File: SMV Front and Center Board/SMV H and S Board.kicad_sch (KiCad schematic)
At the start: 55 parts, among them J1 430450200, J10 Molex Micro-Fit 4 Pin, J2 430450200, J3 XT60-M, J4 22035035, J7 22035035, J8 22035035, J9 22035035, Q1 PSMN1R8-40YLC_115 - MOSFET, Q3 PSMN1R8-40YLC_115 - MOSFET, U1 UA78M05QDCYRG4Q1, U3 PADS131M04QPWRQ1

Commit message: PCB First Layout
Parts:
- removed C3: 220 nF, symbol Device:C
- removed J8, J9: 22035035, CON_22035035_MOL, symbol SMV_Custom:3-pin Mini Molex Spox
- removed Q3: PSMN1R8-40YLC_115 - MOSFET, LFPAK56_SOT669_NEX, symbol PSMN1R8-40YLC,115:PSMN1R8-40YLC_115
- added C1: C0805C224K3RACTU, SMV_Passives:Cap0805, symbol SMV_Custom:C0805C224K3RACTU
- added J5, J6: 22035035, SMV_Connectors:3pin_CON_22035035_MOL, symbol SMV_Custom:3-pin Mini Molex Spox
- added Q2: PSMN1R8-40YLC_115, LFPAK56_SOT669_NEX, symbol PSMN1R8-40YLC,115:PSMN1R8-40YLC_115
- added TP17, TP18: 3V3A, TestPoint:TestPoint_Pad_D3.0mm, symbol Connector:TestPoint
- J4, J7: footprint CON_22035035_MOL -> SMV_Connectors:3pin_CON_22035035_MOL
- Q1: value PSMN1R8-40YLC_115 - MOSFET -> PSMN1R8-40YLC_115
- TP11, TP16: value TestPoint -> 3V3A; footprint (none) -> TestPoint:TestPoint_Pad_D3.0mm
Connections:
- net +3.3V: now also J7.1
- net +3V3: now also RP2040.26 (3.3V), RP2040.27 (3.3V); no longer RP2040.14, RP2040.15
- net CAN_H: now also RP2040.31 (CAN_H), J5.1, J6.1, TP18.1; no longer J7.1, RP2040.1
- net CAN_L: now also RP2040.29 (CAN_L), TP16.1, J5.3, J6.3; no longer J7.3, RP2040.3
- net D1: now also Q2.5; no longer Q1.5
- net D2: now also Q1.5
- net D25: now also RP2040.19 (D25); no longer RP2040.7
- net D4: now also RP2040.13 (D4); no longer RP2040.1
- net GND: now also Q1.1, Q1.2, Q1.3, RP2040.25 (GND), RP2040.30 (GND), C1.2, J5.2, J6.2; no longer RP2040.13, RP2040.2
- net GND - S: now also Q2.1, Q2.2, Q2.3; no longer Q1.1, Q1.2, Q1.3
- net MISO: now also RP2040.16 (MISO), TP17.1; no longer RP2040.4, TP16.1
- net MOSI: now also RP2040.17 (MOSI); no longer RP2040.5
- net SCLK: now also RP2040.18 (SCK); no longer RP2040.6
- net at R2.2, R7.2: now also Q1.4
- net at U3.18 (CAP): now also C1.1
- net at R13.1, TP13.1: now also J4.3
- net at R15.2, TP14.1: now also J7.3; no longer J4.3
- net at R12.2: now also RP2040.23 (A1); no longer RP2040.11
- net at R11.2: now also RP2040.24 (A0); no longer RP2040.12
- net at R3.1, R8.2: now also Q2.4; no longer Q1.4
- no-connect marks 16 -> 15

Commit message: PCB Layout Draft and Small Schematic Changes
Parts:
- added TP19, TP20, TP21: 3V3A, TestPoint:TestPoint_Pad_D3.0mm, symbol Connector:TestPoint
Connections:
- net CS: now also RP2040.21 (A3), TP19.1; no longer RP2040.4 (D13)
- net GND: now also D2.1
- net MISO: now also RP2040.22 (A2); no longer RP2040.16 (MISO)
- net MOSI: now also RP2040.23 (A1); no longer RP2040.17 (MOSI)
- net SCLK: now also TP21.1
- net GPIO_RESET: now reaches RP2040.20 (D24)
- net GPIO_RESET: now also U3.11 (SYNC/RESET), TP20.1
- net at R12.2: now also RP2040.9 (D6); no longer RP2040.23 (A1)
- net at R11.2: now also RP2040.7 (D10); no longer RP2040.24 (A0)
- net D12: now reaches RP2040.5 (D12)
- net D12: now also R8.1
- net D25: no longer names the net of RP2040.19 (D25)
- net D25: no longer R7.1
- net D4: no longer names the net of RP2040.13 (D4)
- net D4: no longer R8.1
- net PWM_OUT: no longer names the net of RP2040.12 (SDA)
- net PWM_OUT: no longer U3.17 (CLKIN)
- net TX1 renamed D11
- net D11: now also R7.1; no longer U3.11 (SYNC/RESET)
- new net GPIO_CLKIN: RP2040.24 (A0), U3.17 (CLKIN)
- no-connect marks 15 -> 9
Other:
- moved on the sheet: D1, D2, R11, R12

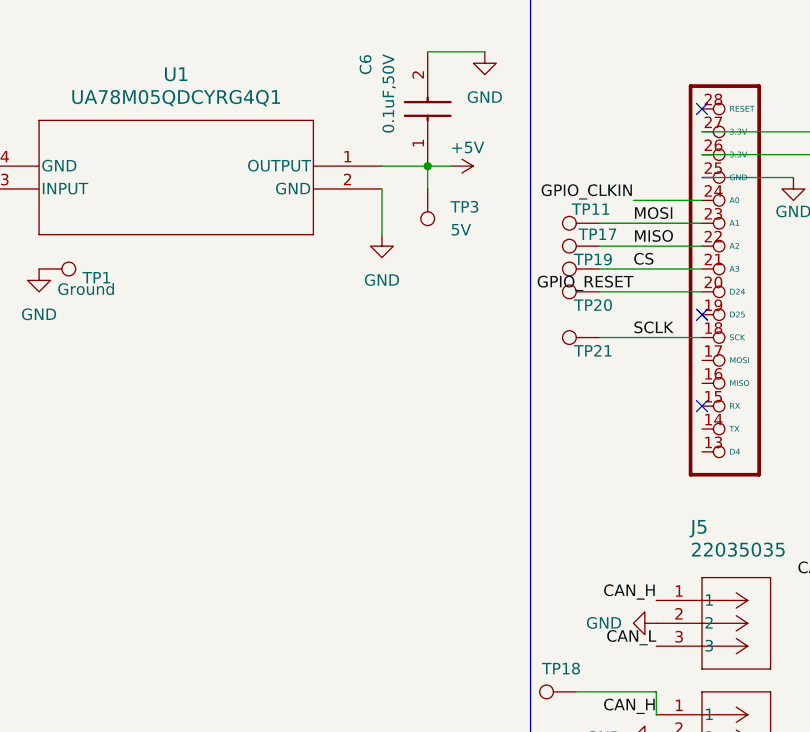
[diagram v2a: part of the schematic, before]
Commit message: Formed compact subsystems
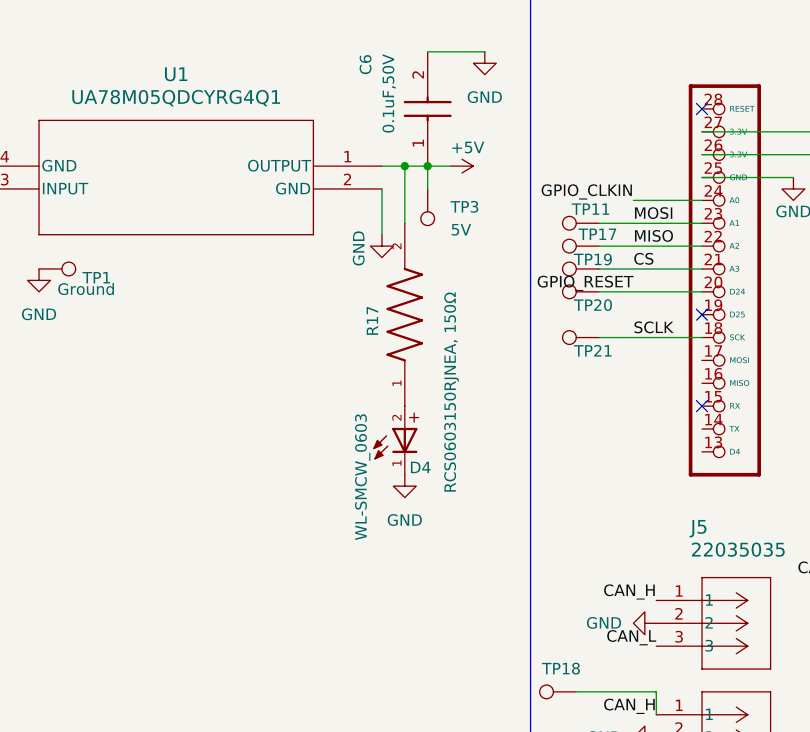
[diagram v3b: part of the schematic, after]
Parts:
- added D4: WL-SMCW_0603, SMV_Passives:WL-SMCW_0603(diode), symbol SMV_Custom:WL-SMCW_0603
- added R17: RCS0603150RJNEA, 150Ω, SMV_Passives:0805RESC2012X60N, symbol SMV_Custom:RCS0603150RJNEA
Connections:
- net +5V: now also R17.2
- net GND: now also D4.1
- new net: D4.2, R17.1
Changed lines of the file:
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@@
 	)
 	(junction
+		(at 91.44 39.37)
+		(diameter 0)
+		(color 0 0 0 0)
+	)
+	(junction
 		(at 204.47 93.98)
 		(diameter 0)
@@
 	(wire
 		(pts
+			(xy 91.44 39.37) (xy 93.98 39.37)
+		)
+		(stroke
+			(width 0)
+			(type default)
+		)
+	)
+	(wire
+		(pts
 			(xy 40.64 187.96) (xy 43.18 187.96)
 		)
@@
 	(wire
 		(pts
+			(xy 91.44 39.37) (xy 91.44 45.72)
+		)
+		(stroke
+			(width 0)
+			(type default)
+		)
+	)
+	(wire
+		(pts
 			(xy 173.99 36.83) (xy 173.99 43.18)
 		)
@@
 	(wire
 		(pts
-			(xy 88.9 39.37) (xy 93.98 39.37)
+			(xy 88.9 39.37) (xy 91.44 39.37)
 		)
 		(stroke
@@
 	)
 	(symbol
+		(lib_id "SMV_Custom:WL-SMCW_0603")
+		(at 91.44 71.12 90)
+		(unit 1)
+		(exclude_from_sim no)
+		(in_bom yes)
+		(on_board yes)
+		(dnp no)
+		(property "Reference" "D4"
+			(at 91.948 72.898 90)
+			(effects
+				(font
+					(size 1.27 1.27)
+				)
+				(justify right)
+			)
+		)
+		(property "Value" "WL-SMCW_0603"
+			(at 86.614 66.802 0)
+			(effects
+				(font
+					(size 1.27 1.27)
+				)
+				(justify right)
+			)
+		)
+		(property "Footprint" "SMV_Passives:WL-SMCW_0603(diode)"
+			(at 91.44 71.12 0)
+			(effects
+				(font
+					(size 1.27 1.27)
+				)
+				(justify bottom)
+				(hide yes)
+			)
+		)
+		(property "Datasheet" ""
+			(at 91.44 71.12 0)
+			(effects
+				(font
+					(size 1.27 1.27)
+				)
+				(hide yes)
+			)
+		)
+		(property "Description" ""
+			(at 91.44 71.12 0)
+			(effects
+				(font
+					(size 1.27 1.27)
+				)
+				(hide yes)
+			)
+		)
+		(pin "1"
+		)
+		(pin "2"
+		)
+		(instances
+			(project "SMV H and S Board"
+				(path "/65429182-9298-499e-afe0-28215a09a0c3"
+					(reference "D4")
+					(unit 1)
+				)
+			)
+		)
+	)
+	(symbol
 		(lib_id "power:GND")
 		(at 204.47 99.06 0)
@@
 		)
 		(property "Value" "GND"
-			(at 88.9 52.07 0)
+			(at 86.36 48.514 90)
 			(effects
 				(font
@@
 	)
 	(symbol
+		(lib_id "SMV_Custom:RCS0603150RJNEA")
+		(at 91.44 55.88 90)
+		(unit 1)
+		(exclude_from_sim no)
+		(in_bom yes)
+		(on_board yes)
+		(dnp no)
+		(property "Reference" "R17"
+			(at 87.884 54.864 0)
+			(effects
+				(font
+					(size 1.27 1.27)
+				)
+				(justify right)
+			)
+		)
+		(property "Value" "RCS0603150RJNEA, 150Ω"
+			(at 96.52 53.34 0)
+			(effects
+				(font
+					(size 1.27 1.27)
+				)
+				(justify right)
+			)
+		)
+		(property "Footprint" "SMV_Passives:0805RESC2012X60N"
+			(at 91.44 55.88 0)
+			(effects
+				(font
+					(size 1.27 1.27)
+				)
+				(justify bottom)
+				(hide yes)
+			)
+		)
+		(property "Datasheet" ""
+			(at 91.44 55.88 0)
+			(effects
+				(font
+					(size 1.27 1.27)
+				)
+				(hide yes)
+			)
+		)
+		(property "Description" ""
+			(at 91.44 55.88 0)
+			(effects
+				(font
+					(size 1.27 1.27)
+				)
+				(hide yes)
+			)
+		)
+		(pin "1"
+		)
+		(pin "2"
+		)
+		(instances
+			(project "SMV H and S Board"
+				(path "/65429182-9298-499e-afe0-28215a09a0c3"
+					(reference "R17")
+					(unit 1)
+				)
+			)
+		)
+	)
+	(symbol
 		(lib_id "power:+VSW")
 		(at 168.91 182.88 0)
@@
 					(unit 1)
 				)
+			)
+		)
+	)
+	(symbol
+		(lib_id "power:GND")
+		(at 91.44 73.66 0)
+		(mirror y)
+		(unit 1)
+		(exclude_from_sim no)
+		(in_bom yes)
+		(on_board yes)
+		(dnp no)
+		(property "Reference" "#PWR039"
+			(at 91.44 80.01 0)
+			(effects
+				(font
+					(size 1.27 1.27)
+				)
+				(hide yes)
+			)
+		)
+		(property "Value" "GND"
+			(at 91.44 78.74 0)
+			(effects
+				(font
+					(size 1.27 1.27)
+				)
+			)
+		)
+		(property "Footprint" ""
+			(at 91.44 73.66 0)
+			(effects
+				(font
+					(size 1.27 1.27)
+				)
+				(hide yes)
+			)
+		)
+		(property "Datasheet" ""
+			(at 91.44 73.66 0)
+			(effects
+				(font
+					(size 1.27 1.27)
+				)
+				(hide yes)
+			)
+		)
+		(property "Description" "Power symbol creates a global label with name \"GND\" , ground"
+			(at 91.44 73.66 0)
+			(effects
+				(font
+					(size 1.27 1.27)
+				)
+				(hide yes)
+			)
+		)
+		(pin "1"
+		)
+		(instances
+			(project "SMV H and S Board"
+				(path "/65429182-9298-499e-afe0-28215a09a0c3"
+					(reference "#PWR039")
+					(unit 1)
+				)

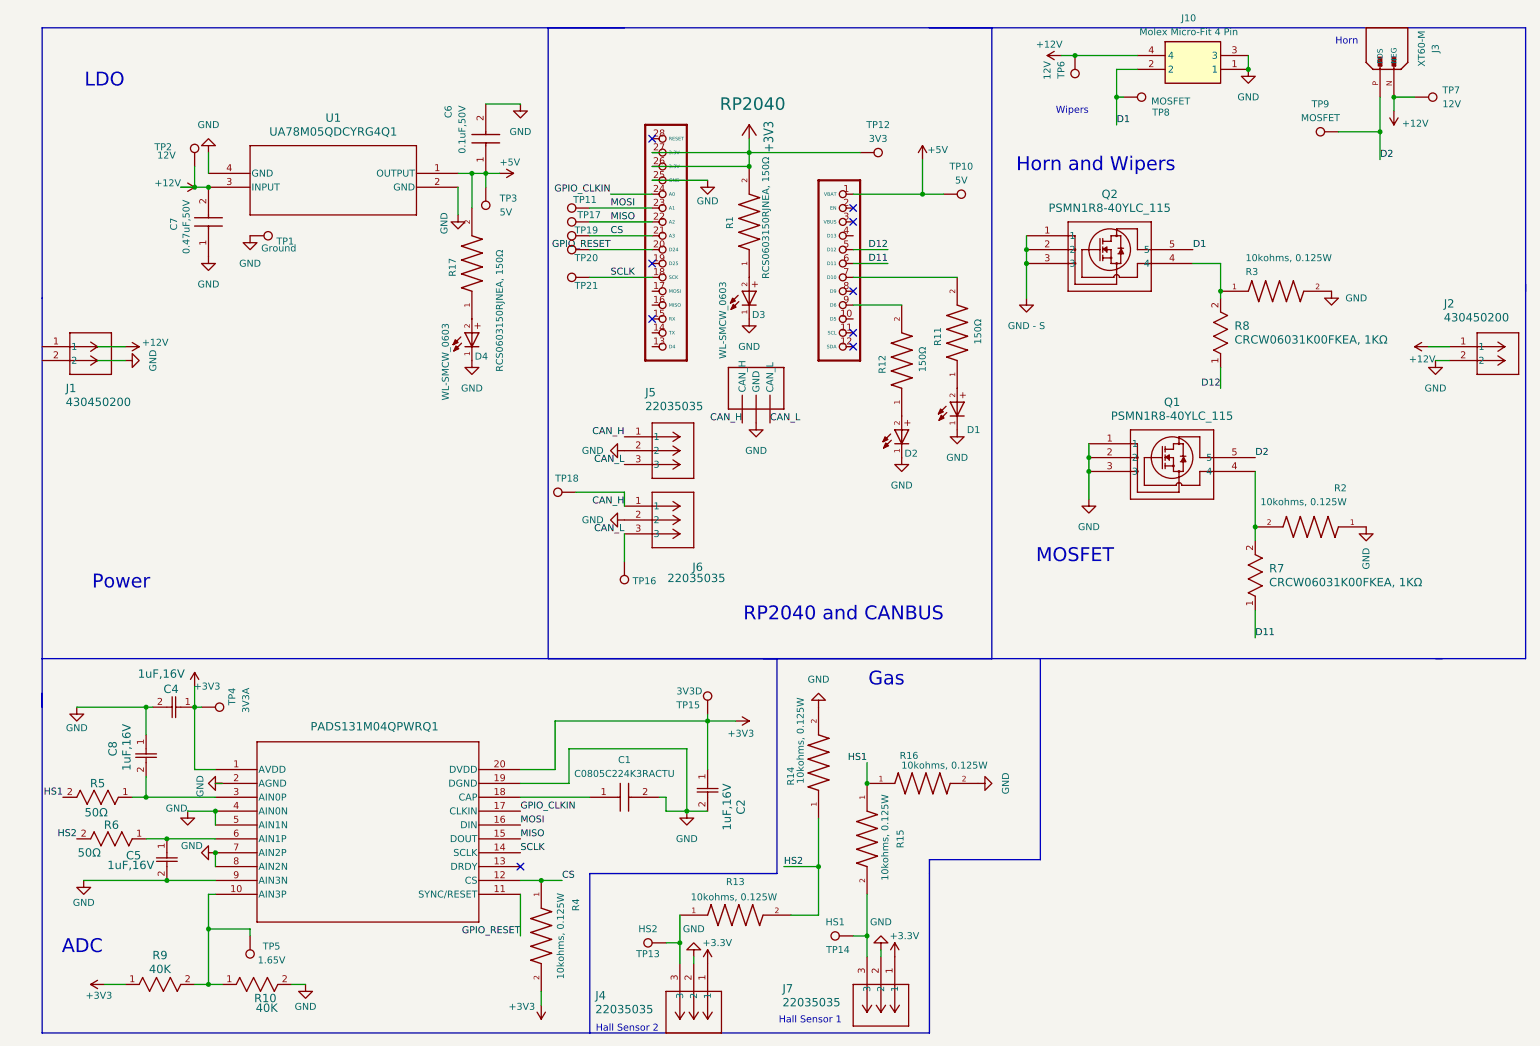
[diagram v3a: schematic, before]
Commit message: Added buffer and reorganized components
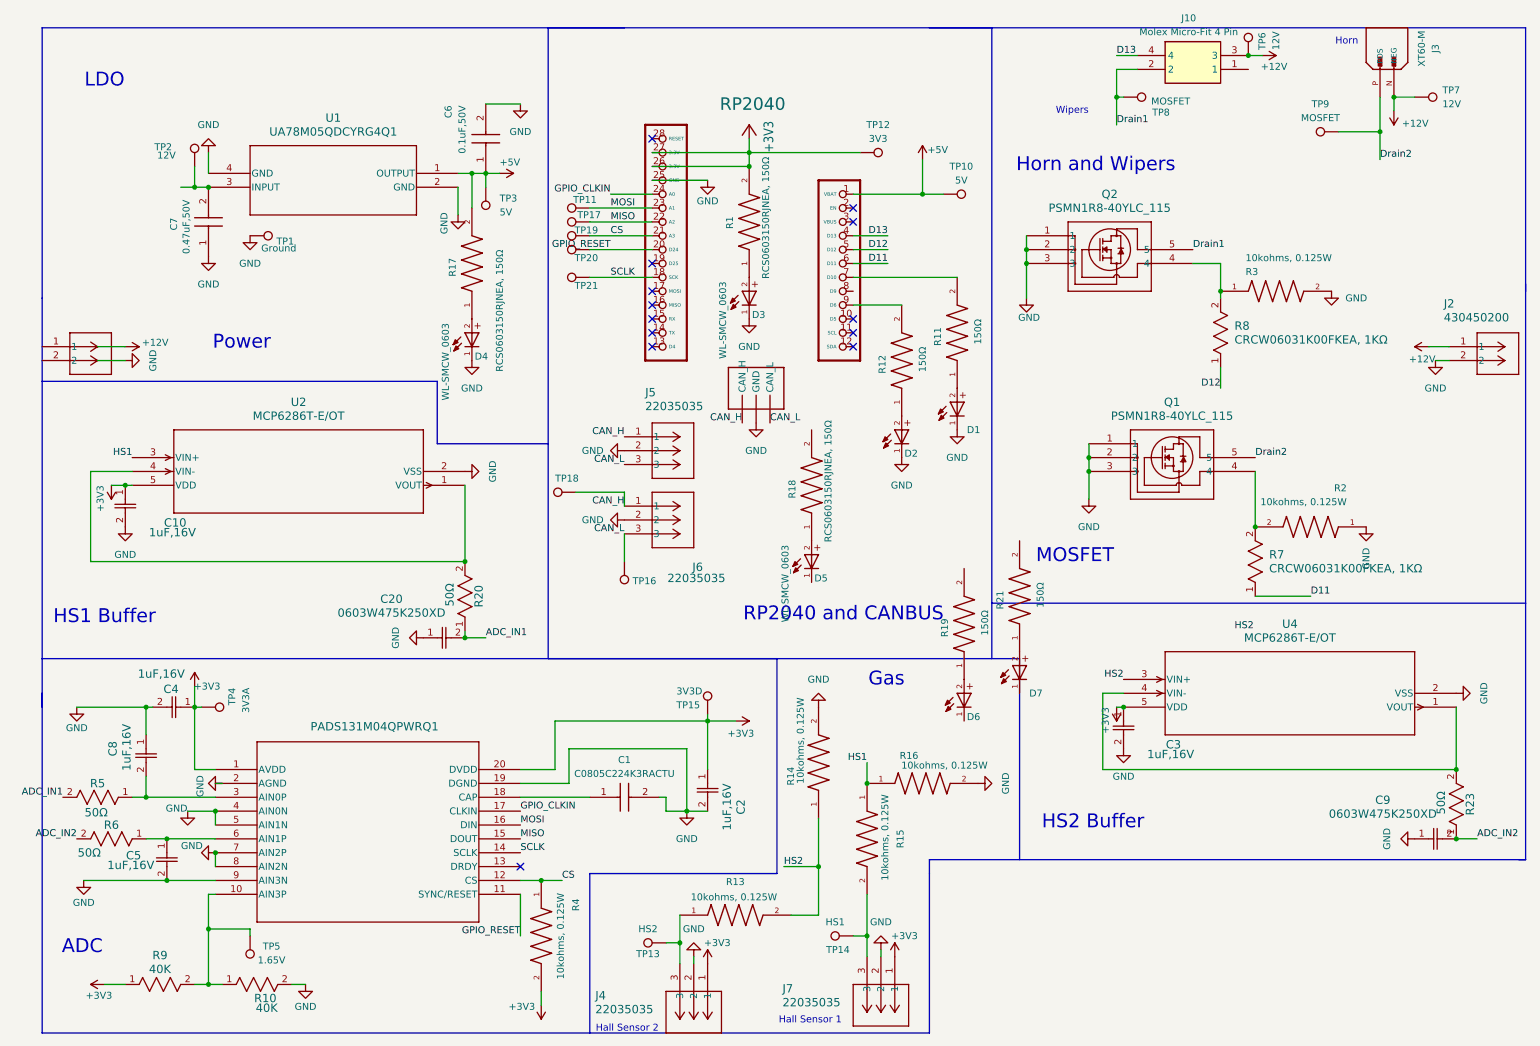
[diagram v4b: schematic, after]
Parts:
- added C10, C3: 1uF,16V, SMV_Passives:Cap0805, symbol SMV_Custom:C0805C105K4RACTU
- added C20, C9: 0603W475K250XD, SMV_Passives:CAP_0603-X_NGC, symbol SMV_Custom:0603W475K250XD
- added D5, D6, D7: WL-SMCW_0603, SMV_Passives:WL-SMCW_0603(diode), symbol SMV_Custom:WL-SMCW_0603
- added R18: RCS0603150RJNEA, 150Ω, SMV_Passives:0805RESC2012X60N, symbol SMV_Custom:RCS0603150RJNEA
- added R19, R21: 150Ω, SMV_Passives:0805RESC2012X60N, symbol SMV_Custom:RCS0603150RJNEA
- added R20, R23: 50Ω, SMV_Passives:0805RESC2012X60N, symbol SMV_Custom:CRCW020149R9FNED
- added U2, U4: MCP6286T-E/OT, SMV_ICs:SOT-23-5_MC_MCH, symbol SMV_Custom:MCP6286T-E_OT
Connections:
- net +3.3V is gone; now on net +3V3: J4.1, J7.1
- net GND - S is gone; now on net GND: Q2.1, Q2.2, Q2.3
- net +12V: now also J10.3; no longer C7.2, J10.4, TP2.1, U1.3 (INPUT)
- net +3V3: now also C10.1, C3.1, U2.5 (VDD), U4.5 (VDD)
- net GND: now also C10.2, C20.1, C3.2, C9.1, U2.2 (VSS), U4.2 (VSS); no longer J10.1, J10.3
- net HS1: now also U2.3 (VIN+); no longer R5.2
- net HS2: now also U4.3 (VIN+); no longer R6.2
- net D13: now reaches RP2040.4 (D13)
- net D13: now also J10.4
- net D1 renamed Drain1
- net D2 renamed Drain2
- new net: D6.2, R19.1
- new net: C7.2, TP2.1, U1.3 (INPUT)
- new net: R20.2, U2.1 (VOUT), U2.4 (VIN-)
- new net: R23.2, U4.1 (VOUT), U4.4 (VIN-)
- new net: D5.2, R18.1
- new net: D7.2, R21.1
- new net ADC_IN1: C20.2, R20.1, R5.2
- new net ADC_IN2: C9.2, R23.1, R6.2
- no-connect marks 9 -> 13
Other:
- note added: "HS1 Buffer"
- note added: "HS2 Buffer"
- moved on the sheet: R7

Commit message: Reorganized
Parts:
- removed D5, D6, D7: WL-SMCW_0603, SMV_Passives:WL-SMCW_0603(diode), symbol SMV_Custom:WL-SMCW_0603
- removed R18: RCS0603150RJNEA, 150Ω, SMV_Passives:0805RESC2012X60N, symbol SMV_Custom:RCS0603150RJNEA
- removed R19, R21: 150Ω, SMV_Passives:0805RESC2012X60N, symbol SMV_Custom:RCS0603150RJNEA
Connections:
- net +12V: now also C7.2, J1.2, TP2.1, U1.3 (INPUT)
- net GND: now also J1.1
- net FB: now reaches R20.2, U2.1 (VOUT), U2.4 (VIN-)

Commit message: Reorganized, added filled zones
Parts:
- removed J3: XT60-M, XT60-M:AMASS_XT60-M, symbol XT60-M:XT60-M
- removed TP20: 3V3A, TestPoint:TestPoint_Pad_D3.0mm, symbol Connector:TestPoint
- added J8: 430450200, SMV_Connectors:CONN_SD-43045-001_02_MOL, symbol SMV_Custom:430450200
- TP11, TP13, TP14, TP16, TP17, TP18, TP19, TP21, TP3, TP5, TP8, TP9: footprint TestPoint:TestPoint_Pad_D3.0mm -> TestPoint:TestPoint_Pad_D1.5mm
- TP15: value 3V3D -> 3V3A; footprint TestPoint:TestPoint_Pad_D3.0mm -> TestPoint:TestPoint_Pad_D1.5mm
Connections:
- net +12V: now also J8.2
- net +3V3: no longer TP15.1
- net CS: now also RP2040.19 (D25); no longer RP2040.21 (A3)
- net Drain2: now also J8.1
- net GPIO_CLKIN: now also TP15.1
- net GPIO_RESET: now also RP2040.17 (MOSI); no longer RP2040.20 (D24)
- no-connect marks 13 -> 14
